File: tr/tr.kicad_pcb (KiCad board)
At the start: 4 copper layers, 104.4 x 65.5 mm, 105 parts, among them J1 SMA, J2 SMA, J3 SMA, K1 CONN_3, Q1 Si7850, Q3 STD2NK90ZT4, Q4 STD2NK90ZT4, T1 DA2033-AL_, U1 L6388E, U2 LT1631, U3 LT3757

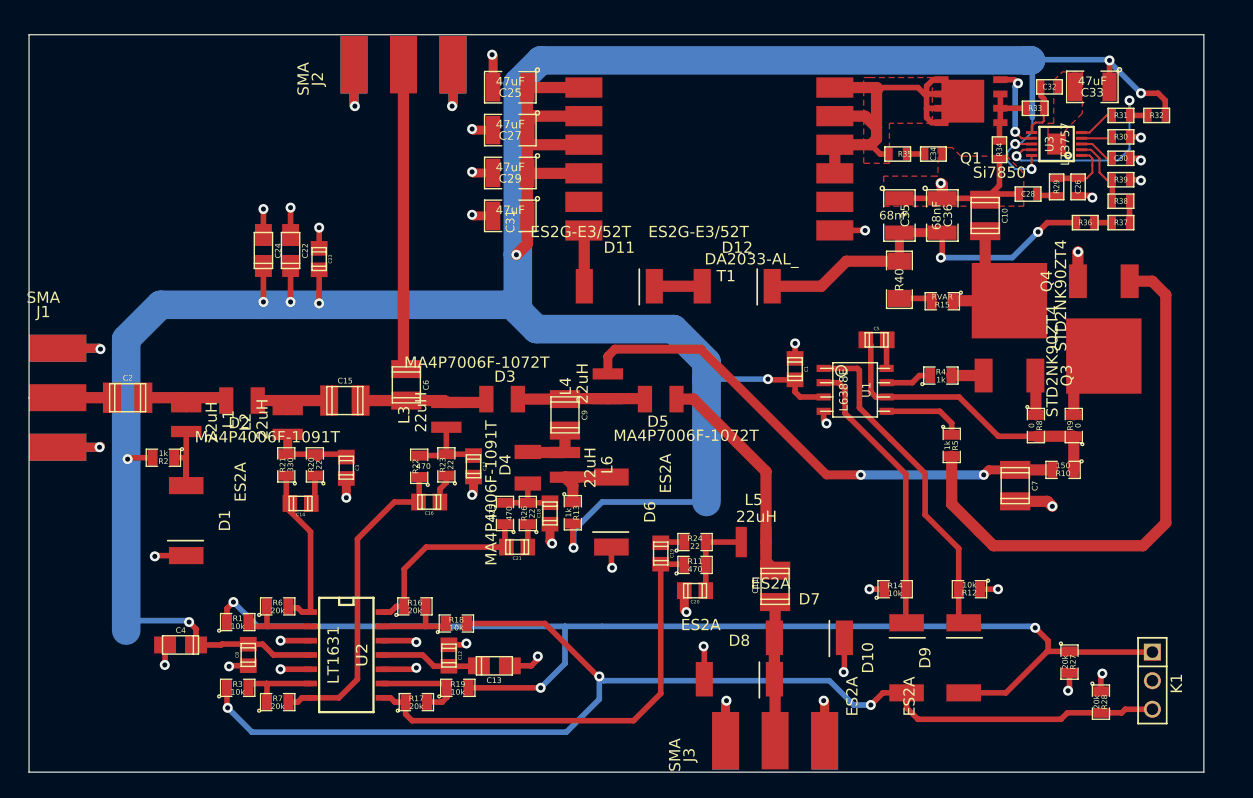
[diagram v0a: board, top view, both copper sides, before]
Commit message: silkscreen layout for tr, updated to kicad 2014.3.13bzr
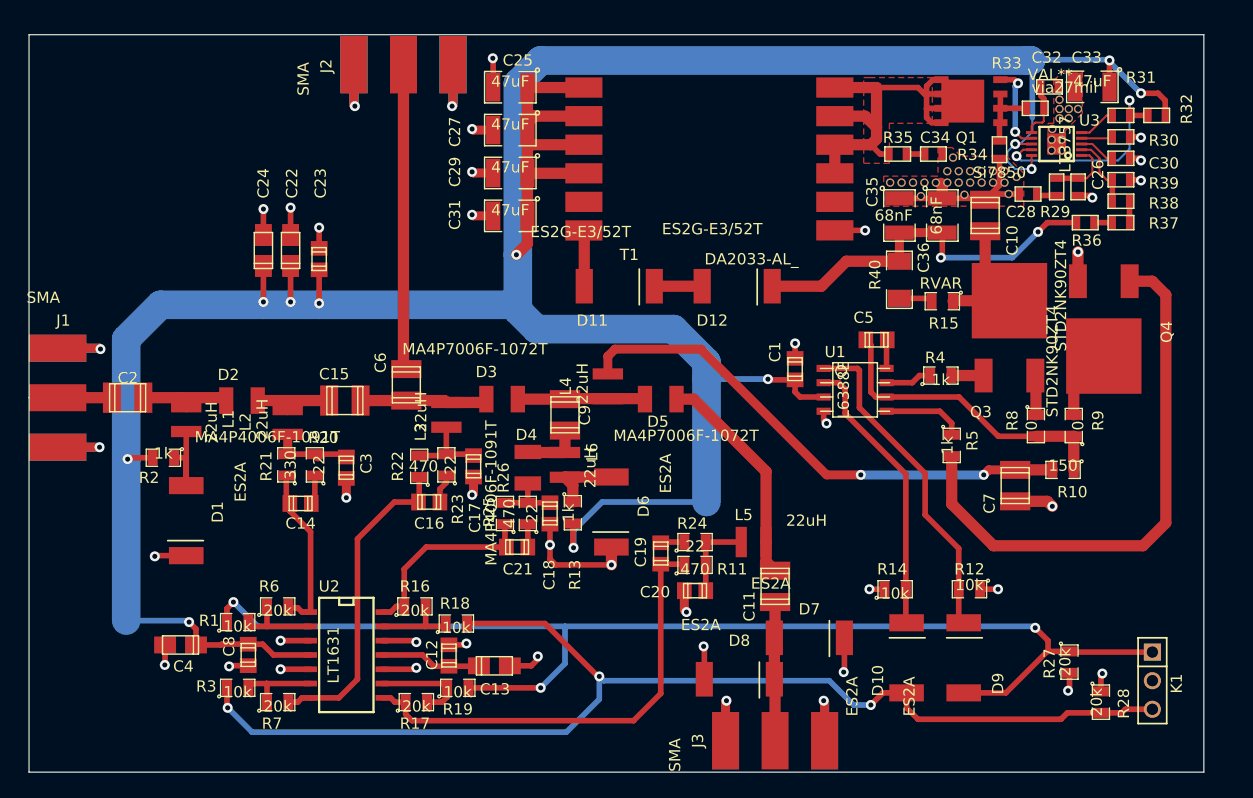
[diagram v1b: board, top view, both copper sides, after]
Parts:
- added ?: , via27mil, F.Cu at (141.8, 37.0)
- added ?: , via27mil, F.Cu at (139.3, 35.8)
- added ?: , via27mil, F.Cu at (144.9, 37.5)
- added ?: , via27mil, F.Cu at (136.4, 39.2)
- added ?: , via27mil, F.Cu at (148.7, 30.7)
- added ?: , via27mil, F.Cu at (149.5, 32.3)
- added ?: , via27mil, F.Cu at (135.7, 38.0)
- added ?: , via27mil, F.Cu at (133.7, 38.0)
- added ?: , via27mil, F.Cu at (143.8, 38.0)
- added ?: , via27mil, F.Cu at (144.2, 39.1)
- added ?: , via27mil, F.Cu at (137.7, 38.0)
- added ?: , via27mil, F.Cu at (140.8, 37.0)
- added ?: , via27mil, F.Cu at (138.7, 38.0)
- added ?: , via27mil, F.Cu at (136.7, 38.0)
- added ?: , via27mil, F.Cu at (150.4, 31.5)
- added ?: , via27mil, F.Cu at (143.8, 37.0)
- added ?: , via27mil, F.Cu at (142.8, 37.0)
- added ?: , via27mil, F.Cu at (134.7, 38.0)
- added ?: , via27mil, F.Cu at (149.5, 31.5)
- added ?: , via27mil, F.Cu at (148.7, 31.5)
- added ?: , via27mil, F.Cu at (148.1, 33.3)
- added ?: , via27mil, F.Cu at (151.1, 26.1)
- added ?: , via27mil, F.Cu at (138.7, 37.0)
- added ?: , via27mil, F.Cu at (148.0, 35.2)
- added ?: , via27mil, F.Cu at (148.9, 35.2)
- added ?: , via27mil, F.Cu at (148.9, 34.2)
- added ?: , via27mil, F.Cu at (148.0, 34.2)
- added ?: , via27mil, F.Cu at (148.7, 32.3)
- added ?: , via27mil, F.Cu at (139.8, 37.0)
- added ?: , via27mil, F.Cu at (142.8, 38.0)
- added ?: , via27mil, F.Cu at (141.8, 38.0)
- added ?: , via27mil, F.Cu at (139.8, 38.0)
- added ?: , via27mil, F.Cu at (140.8, 38.0)
- added ?: , via27mil, F.Cu at (140.3, 39.1)
- added via27mil: VAL**, via27mil, F.Cu at (148.8, 30.6)
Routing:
- net GND: track 132.6 -> 144.2 mm, vias 43 -> 42
- net VCC: track 294.9 -> 289.2 mm
- net (no net): track 0.64 -> 0.00 mm

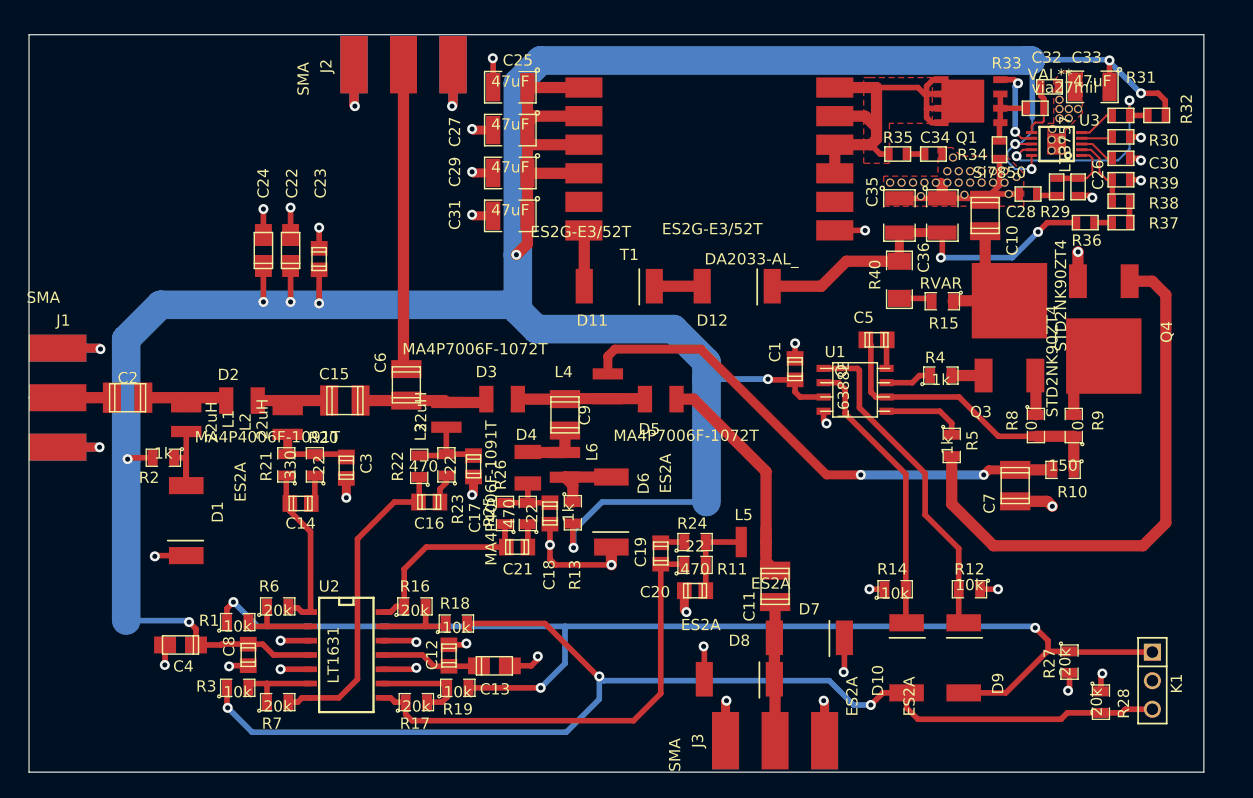
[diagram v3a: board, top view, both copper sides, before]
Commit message: started on t/r with enclosure, migrated distro to 15v
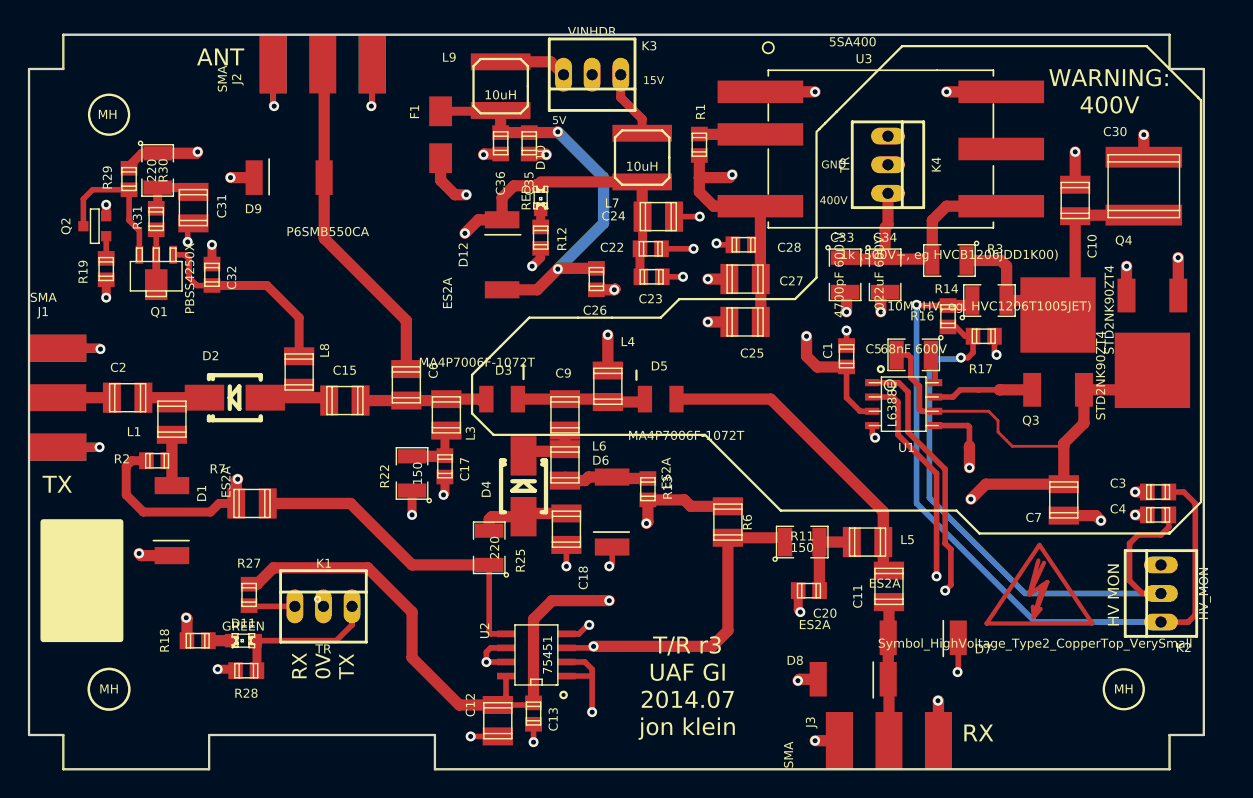
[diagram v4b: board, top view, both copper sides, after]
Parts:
- removed the ? at (141.8, 37.0)
- removed the ? at (139.3, 35.8)
- removed the ? at (144.9, 37.5)
- removed the ? at (136.4, 39.2)
- removed the ? at (148.7, 30.7)
- removed the ? at (149.5, 32.3)
- removed the ? at (135.7, 38.0)
- removed the ? at (133.7, 38.0)
- removed the ? at (143.8, 38.0)
- removed the ? at (144.2, 39.1)
- removed the ? at (137.7, 38.0)
- removed the ? at (140.8, 37.0)
- removed the ? at (138.7, 38.0)
- removed the ? at (136.7, 38.0)
- removed the ? at (150.4, 31.5)
- removed the ? at (143.8, 37.0)
- removed the ? at (142.8, 37.0)
- removed the ? at (134.7, 38.0)
- removed the ? at (149.5, 31.5)
- removed the ? at (148.7, 31.5)
- removed the ? at (148.1, 33.3)
- removed the ? at (151.1, 26.1)
- removed the ? at (138.7, 37.0)
- removed the ? at (148.0, 35.2)
- removed the ? at (148.9, 35.2)
- removed the ? at (148.9, 34.2)
- removed the ? at (148.0, 34.2)
- removed the ? at (148.7, 32.3)
- removed the ? at (139.8, 37.0)
- removed the ? at (142.8, 38.0)
- removed the ? at (141.8, 38.0)
- removed the ? at (139.8, 38.0)
- removed the ? at (140.8, 38.0)
- removed the ? at (140.3, 39.1)
- removed C14, C16, C19, C21: 100pF, c_0805
- removed C29: 47uF, SM1210
- removed C8: 10nF, c_0805
- removed L2: 22uH, l_3x3
- removed R10: 150, SM0805
- removed R15: RVAR, SM0805
- removed R20, R23, R24, R26: 22, SM0805
- removed R21: 330, SM0805
- removed R32: 105k, SM0603
- removed R33, R35: 22, SM0603
- removed R34: .02, SM0603
- removed R36: 1.5M, SM0603
- removed R37, R38: 1M, SM0603
- removed R39: 16.2k, SM0603
- removed R4, R5: 1k, SM0805
- removed R40: 1M, SM1206
- removed R8, R9: 0, SM0805
- removed T1: DA2033-AL_, DA2033-AL
- removed via27mil: VAL**, via27mil
- added ?: Symbol_HighVoltage_Type2_CopperTop_VerySmall, Footprint_Symbols:Symbol_HighVoltage_Type2_CopperTop_VerySmall, F.Cu at (146.9, 74.4)
- added F1: PTC FUSE (0ZCJ0010FF2E), Fuse_Holders_and_Fuses:Fuse_SMD1206_HandSoldering, F.Cu at (93.7, 33.8)
- added K2: HV_MON, Connect:PINHEAD1-3, F.Cu at (157.7, 74.5)
- added K3: VINHDR, Connect:PINHEAD1-3, F.Cu at (107.2, 28.4)
- added K4: TR, Connect:PINHEAD1-3, F.Cu at (133.5, 36.4)
- added L7: 10uH, Inductors:SELF-WE-TPC_M, F.Cu at (111.6, 35.8)
- added L8: 22uH, smd_capacitors:c_1210, F.Cu at (81.2, 54.9)
- added L9: 10uH, Inductors:SELF-WE-TPC_M, F.Cu at (99.1, 29.5)
- added MH: MountingHole_3-5mm_RevA_Date21Jun2010, Mounting_Holes:MountingHole_3-5mm, F.Cu at (154.4, 83.1)
- added MH: MountingHole_3-5mm_RevA_Date21Jun2010, Mounting_Holes:MountingHole_3-5mm, F.Cu at (64.3, 83.1)
- added MH: MountingHole_3-5mm_RevA_Date21Jun2010, Mounting_Holes:MountingHole_3-5mm, F.Cu at (64.3, 32.0)
- added Q2: MMBT2222A, SMD_Packages:SOT23EBC, F.Cu at (63.0, 41.9)
- C1, C17, C20, C23, C3: footprint c_0805 -> smd_capacitors:c_0805
- C10: value .022uF -> 4700pF 600V; footprint c_1210 -> smd_capacitors:c_1210
- C11, C7, C9: value .022uF -> .022uF, 600 V; footprint c_1210 -> smd_capacitors:c_1210
- C12: value 10nF -> 22uF; footprint c_0805 -> Capacitors_SMD:c_1210
- C13: value 2.2uF -> 100nF; footprint c_tant_A -> smd_capacitors:c_0805
- C15, C2, C6: value .022uF -> .022uF 600 V; footprint c_1210 -> smd_capacitors:c_1210
- C18: footprint c_0805 -> smd_capacitors:c_1210
- C22: footprint c_tant_A -> smd_capacitors:c_0805
- C24: value 10uF -> 22uF; footprint c_tant_A -> smd_capacitors:c_1210
- C25, C27, C31: value 47uF -> 22uF; footprint SM1210 -> smd_capacitors:c_1210
- C26: value 100pF -> 100nF; footprint SM0603 -> smd_capacitors:c_0805
- C28: value 22nF -> 100pF; footprint SM0603 -> smd_capacitors:c_0805
- C30: value 100nF -> .47uF 600V; footprint SM0603 -> Capacitors_SMD:c_2225
- C32: footprint SM0603 -> smd_capacitors:c_0805
- C33: value 47uF -> 4700pF 600 V; footprint SM1210 -> SMD_Packages:SMD-1210
- C34: value 220pF -> .022uF 600V; footprint SM0603 -> SMD_Packages:SMD-1210
- C35: value 68nF -> 10nF; footprint SM1210 -> smd_capacitors:c_0805
- C36: value 68nF -> 2.2uF; footprint SM1210 -> smd_capacitors:c_0805
- C4: value 2.2uF -> 10nF; footprint c_tant_A -> smd_capacitors:c_0805
- C5: value 68nF -> 68nF 600V; footprint c_0805 -> SMD_Packages:SMD-1210
- D1, D6, D7, D8: footprint SMB_DO2144AA -> smb_diode:SMB_DO2144AA
- D10: value ES2A -> RED; footprint SMB_DO2144AA -> LEDs:LED-0805
- D11: value ES2G-E3/52T -> GREEN; footprint SMB_DO2144AA -> LEDs:LED-0805
- D12: value ES2G-E3/52T -> ES2A; footprint SMB_DO2144AA -> smb_diode:SMB_DO2144AA
- D2, D4: footprint MELF-1072 -> Diodes_SMD:Diode-SMB_Handsoldering
- D3, D5: footprint MELF-1072 -> melf-1072:MELF-1072
- D9: value ES2A -> P6SMB550CA; footprint SMB_DO2144AA -> smb_diode:SMB_DO2144AA
- J1, J2, J3: footprint sma -> sma:sma
- K1: value CONN_3 -> TR; footprint PIN_ARRAY_3X1 -> Connect:PINHEAD1-3
- L1, L3, L4, L5, L6: footprint l_3x3 -> smd_capacitors:c_1210
- Q1: value Si7850 -> PBSS4250X; footprint SO8PowerPAK -> Transistors_SMD:sot89
- Q3, Q4: footprint TO252-3 -> to252:TO252-3
- R1, R12, R13, R18, R19, R2: footprint SM0805 -> smd_capacitors:c_0805
- R11, R22: value 470 -> 150; footprint SM0805 -> SMD_Packages:SMD-1210
- R14: value 10k -> 10M (HV, eg. HVC1206T1005JET); footprint SM0805 -> SMD_Packages:SM1210
- R16: value 20k -> 5k1; footprint SM0805 -> smd_capacitors:c_0805
- R17, R27, R28: value 20k -> 10k; footprint SM0805 -> smd_capacitors:c_0805
- R25: value 470 -> 220; footprint SM0805 -> SMD_Packages:SMD-1210
- R29: value 6.8k -> 510; footprint SM0603 -> smd_capacitors:c_0805
- R3: value 10k -> 1k (500V+, eg HVCB1206JDD1K00); footprint SM0805 -> SMD_Packages:SM1210
- R30: value 140k -> 220; footprint SM0603 -> SMD_Packages:SMD-1210
- R31: value 46.4k -> 22; footprint SM0603 -> smd_capacitors:c_0805
- R6, R7: value 20k -> 300 (1W); footprint SM0805 -> smd_capacitors:c_1210
- U1: footprint so-8 -> smd_dil:so-8
- U2: value LT1631 -> 75451; footprint SO14N -> SOIC_Packages:SOIC-8_N
- U3: value LT3757 -> 5SA400; footprint MSOP10EP-0.5 -> PICOPSU:xxSAxxxx
- moved C4 87.6 mm to (157.5, 67.6)
- moved R31 86.2 mm to (68.5, 41.3), turned to 90 degrees
- moved R30 85.7 mm to (68.6, 37.0), turned to 270 degrees
- moved R29 82.4 mm to (66.0, 37.7)
- moved C32 76.3 mm to (73.4, 46.2), turned to 90 degrees
- moved R28 76.0 mm to (76.5, 81.4), turned to 180 degrees
- moved Q1 74.0 mm to (68.5, 46.4)
- moved K1 74.0 mm to (83.3, 75.7), turned to 0 degrees
- moved R3 73.8 mm to (138.9, 45.0), turned to 180 degrees
- moved D9 73.6 mm to (80.3, 37.6), turned to 180 degrees
- moved R27 73.1 mm to (76.7, 74.7)
- moved C3 72.2 mm to (157.5, 65.5), turned to 0 degrees
- moved R17 60.0 mm to (142.0, 51.7), turned to 180 degrees
- moved R1 59.0 mm to (116.7, 34.7), turned to 270 degrees
- moved R16 53.9 mm to (138.8, 49.9), turned to 270 degrees
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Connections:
- C12 pad 1: VEE -> +5V
- C13 pad 1: VEE -> +5V
- C25 pad 1: VCC -> Net-(C25-Pad1)
- C26 pad 1: GND -> +5V
- C26 pad 2: N-0000047 -> GND
- C27 pad 1: VCC -> Net-(C25-Pad1)
- C28 pad 1: GND -> Net-(C25-Pad1)
- C28 pad 2: N-0000049 -> GND
- C3 pad 1: GND -> Net-(C3-Pad1)
- C3 pad 2: N-0000016 -> GND
- C30 pad 1: GND -> VDD
- C30 pad 2: N-0000050 -> GND
- C31 pad 1: VCC -> Net-(C31-Pad1)
- C32 pad 2: N-0000048 -> Net-(C32-Pad2)
- C33 pad 1: VCC -> Net-(C33-Pad1)
- C34 pad 1: GND -> Net-(C33-Pad1)
- C34 pad 2: N-0000033 -> GND
- C35 pad 1: GND -> +5V
- C35 pad 2: N-0000034 -> GND
- C36 pad 1: GND -> +5V
- C36 pad 2: N-0000034 -> GND
- C4 pad 1: VCC -> Net-(C4-Pad1)
- C5 pad 2: /hvout -> /hvbias
- C6 pad 2: N-0000017 -> Net-(C6-Pad2)
- D10 pad 1: /TX -> VCC
- D10 pad 2: N-0000039 -> Net-(D10-Pad2)
- D11 pad 1: N-0000035 -> /TX
- D11 pad 2: N-0000036 -> Net-(D11-Pad2)
- D12 pad 1: N-0000036 -> +5V
- D12 pad 2: N-0000034 -> VCC
- D9 pad 1: /RX -> Net-(C6-Pad2)
- D9 pad 2: N-0000040 -> GND
- J2 pad 1: N-0000017 -> Net-(C6-Pad2)
- Q1 pad 1: N-0000032 -> Net-(C32-Pad2)
- Q1 pad 2: N-0000032 -> Net-(Q1-Pad2)
- Q1 pad 3: N-0000032 -> Net-(Q1-Pad3)
- Q3 pad G: N-0000026 -> Net-(Q3-PadG)
- Q3 pad S: /hvs -> /hvbias
- Q4 pad D: /hvd -> /hvbias
- Q4 pad G: N-0000027 -> Net-(Q4-PadG)
- R1 pad 1: /RX -> Net-(C25-Pad1)
- R1 pad 2: N-000002 -> Net-(R1-Pad2)
- R11 pad 1: /OUTC -> /RXDRV
- R12 pad 1: GND -> Net-(D10-Pad2)
- R12 pad 2: N-0000040 -> GND
- R14 pad 1: GND -> Net-(C3-Pad1)
- R14 pad 2: N-0000039 -> VDD
- R16 pad 1: /OUTD -> Net-(C4-Pad1)
- R16 pad 2: N-000003 -> Net-(C3-Pad1)
- R17 pad 1: /OUTC -> Net-(C4-Pad1)
- R17 pad 2: N-000004 -> GND
- R18 pad 1: N-000003 -> GND
- R18 pad 2: /TX -> Net-(D11-Pad2)
- R19 pad 1: N-000004 -> /RXDRV
- R19 pad 2: /RX -> Net-(Q2-Pad2)
- R22 pad 1: /OUTB -> /RXDRV
- R25 pad 1: /OUTD -> /TXDRV
- R27 pad 2: GND -> +5V
- R29 pad 1: N-0000049 -> VCC
- R29 pad 2: N-0000047 -> Net-(Q1-Pad3)
- R3 pad 1: /TX -> VDD
- R3 pad 2: N-000001 -> Net-(C33-Pad1)
- R30 pad 1: GND -> VCC
- R30 pad 2: N-0000041 -> Net-(C31-Pad1)
- R31 pad 1: N-0000043 -> Net-(C31-Pad1)
- R31 pad 2: N-0000042 -> Net-(Q1-Pad2)
- R6 pad 1: N-000002 -> /RXDRV
- R6 pad 2: /OUTA -> VCC
- R7 pad 1: N-000001 -> /TXDRV
- R7 pad 2: /OUTB -> VCC
- U1 pad 1: N-0000040 -> /RX
- U1 pad 2: N-0000039 -> /TX
- U1 pad 5: N-0000025 -> Net-(Q4-PadG)
- U1 pad 6: /hvout -> /hvbias
- U1 pad 7: N-0000055 -> Net-(Q3-PadG)
- U2 pad 1: /OUTA -> /RX
- U2 pad 2: N-000002 -> /RX
- U2 pad 3: GND -> /RXDRV
- U2 pad 4: VCC -> GND
- U2 pad 5: GND -> /TXDRV
- U2 pad 6: N-000001 -> /TX
- U2 pad 7: /OUTB -> /TX
- U2 pad 8: /OUTC -> +5V
- U3 pad 1: N-0000047 -> GND
- U3 pad 2: N-0000044 -> Net-(R1-Pad2)
- U3 pad 3: N-0000050 -> Net-(C25-Pad1)
- U3 pad 4: N-0000041 -> Net-(C33-Pad1)
- U3 pad 5: N-0000042 -> (no net)
- U3 pad 6: N-0000048 -> GND
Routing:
- net +5V: track 0.00 -> 125.9 mm, vias 0 -> 3
- net /RXDRV: track 0.00 -> 99.6 mm, vias 0 -> 3
- net VCC: track 289.2 -> 196.8 mm, vias 12 -> 5
- net Net-(C3-Pad1): track 0.00 -> 64.9 mm, vias 0 -> 1
- net Net-(C4-Pad1): track 0.00 -> 55.9 mm, vias 0 -> 1
- net Net-(C25-Pad1): track 0.00 -> 55.0 mm, vias 0 -> 2
- net N-0000027: track 49.6 -> 0.00 mm
- net /hvbias: track 46.1 -> 94.5 mm
- net Net-(Q4-PadG): track 0.00 -> 44.0 mm, vias 0 -> 2
- net /OUTC: track 40.9 -> 0.00 mm
- net N-0000038: track 34.7 -> 0.00 mm
- net N-0000034: track 34.2 -> 0.00 mm, vias 2 -> 0
- net Net-(C6-Pad2): track 0.00 -> 30.5 mm
- net N-0000040: track 29.5 -> 0.00 mm
- net /TXDRV: track 0.00 -> 29.5 mm
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- added copper zone on Inner2.Cu, net GND
- removed copper zone on F.Cu, net GND
- removed copper zone on Inner1.Cu, net GND
- removed copper zone on F.Cu, net N-0000038
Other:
- board size 104.4 x 65.5 mm -> 104.4 x 65.3 mm
- rule trace_min: 0.17 -> 0.2
- board text added: "15V"
- board text added: "400V"
- board text added: "5V"
- board text added: "ANT"
- board text added: "GND"
- board text added: "HV MON"
- board text added: "RX"
- board text added: "RX 0V TX"
- board text added: "T/R r3 UAF GI 2014.07 jon klein"
- board text added: "TX"
- board text added: "WARNING: 400V"
- board text added: "high power T/R switch r3"
